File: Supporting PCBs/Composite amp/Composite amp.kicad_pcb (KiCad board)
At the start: 2 copper layers, 31.2 x 23.3 mm, 10 parts, among them J1 Conn_01x14_Female, Q1 MMBT3906

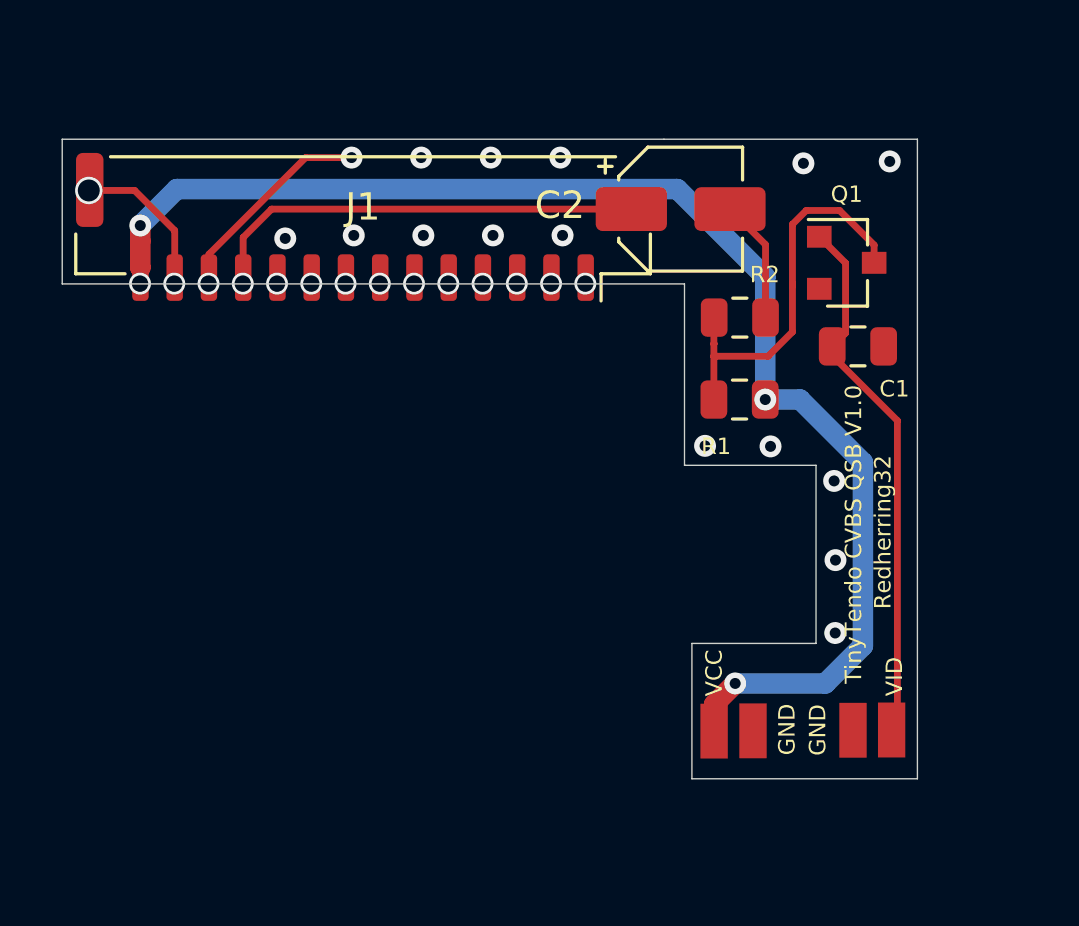
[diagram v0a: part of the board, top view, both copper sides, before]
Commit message: + Updated README.md + Fixed schematic/pinout error with Q1, and added decoupling capacitor to Composite Amp
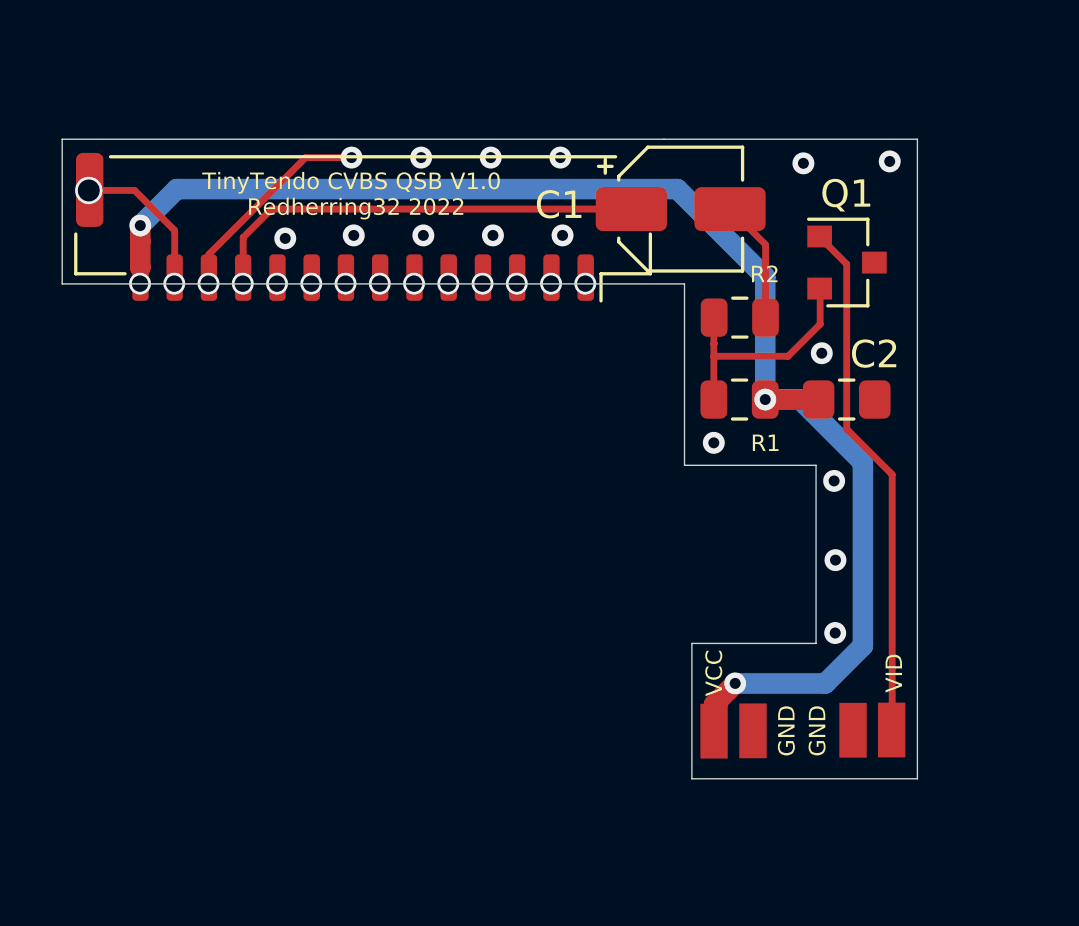
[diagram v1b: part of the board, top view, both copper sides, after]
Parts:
- removed the C1 at (85.7, 70.8)
- added C2: 22uF, Capacitor_SMD:C_0805_2012Metric_Pad1.15x1.40mm_HandSolder, F.Cu at (85.2, 72.7)
- renumbered C2 to C1, GND to GND1, GND to GND2, VCC to VCC1, VID to VID1
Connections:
- Q1 pad 2: /GND -> Net-(Q1-Pad2)
- Q1 pad 3: Net-(Q1-Pad3) -> /GND
- R1 pad 2: Net-(Q1-Pad3) -> Net-(Q1-Pad2)
- R2 pad 2: Net-(Q1-Pad3) -> Net-(Q1-Pad2)
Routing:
- net Net-(Q1-Pad3): track 14.6 -> 0.00 mm
- net Net-(Q1-Pad2): track 0.00 -> 8.68 mm
- net /5V: track 49.2 -> 51.1 mm
- net /VIDEO-IN: track 19.7 -> 19.1 mm
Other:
- board text added: "GND"
- board text added: "Redherring32 2022"
- board text added: "VCC"
- board text added: "VID"
- board text removed: "Redherring32"
